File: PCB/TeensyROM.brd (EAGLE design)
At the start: 160 x 100 mm, 2 parts, among them P1 MA22-2, U1 TEENSY41-STRIP

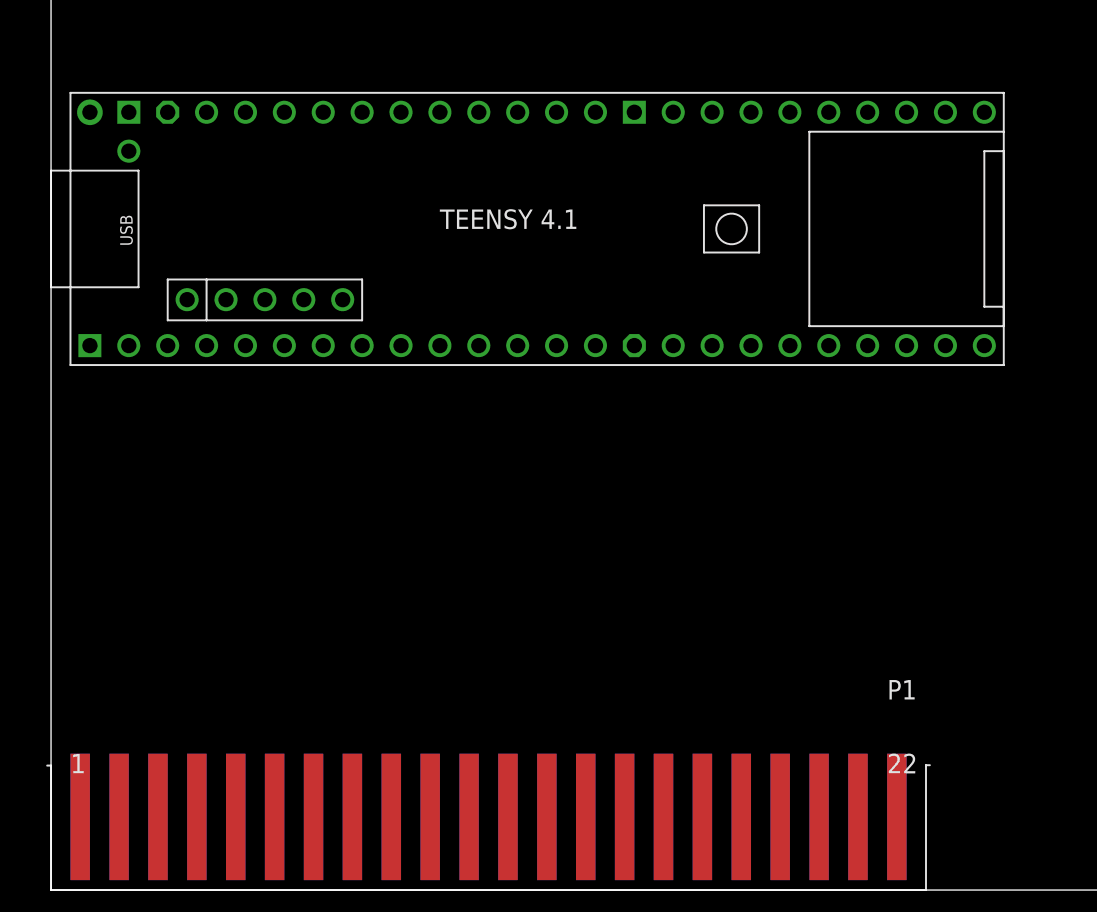
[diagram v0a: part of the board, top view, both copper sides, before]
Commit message: DMA/NMI pins
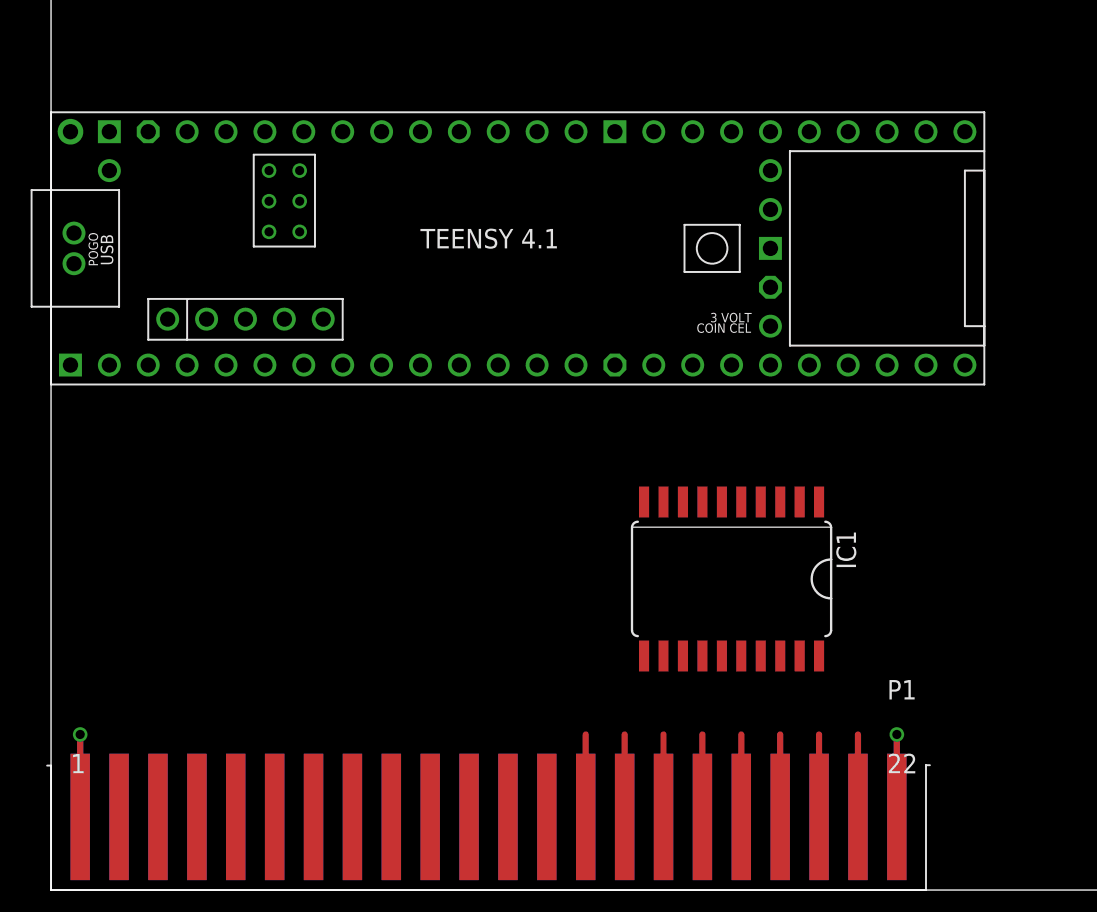
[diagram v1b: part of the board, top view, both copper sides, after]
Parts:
- removed U1: TEENSY41-STRIP, teensy:TEENSY41-STRIP
- added IC1: 74LS245DW, 74xx-us:SO20W
- added U$1: TEENSY41, teensy:TEENSY41
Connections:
- new net *DMA: P1.13
- new net *EXROM: P1.9
- new net *GAME: P1.8
- new net *IO1: P1.7
- new net *IO2: P1.10
- new net *IRQ: P1.4
- new net *NMI: P1.D
- new net *RESET: P1.C
- new net *ROMH: P1.B
- new net *ROML: P1.11
- new net +5V: P1.2, P1.3
- new net A0: P1.Y
- new net A1: P1.X
- new net A10: P1.M
- new net A11: P1.L
- new net A12: P1.K
- new net A13: P1.J
- new net A14: P1.H
- new net A15: P1.F
- new net A2: P1.W
- new net A3: P1.V
- new net A4: P1.U
- new net A5: P1.T
- new net A6: P1.S
- new net A7: P1.R
- new net A8: P1.P
- new net A9: P1.N
- new net BA: P1.12
- new net D0: IC1.18, P1.21
- new net D0_B: IC1.2, U$1.10-CS\MQSR
- new net D1: IC1.17, P1.20
- new net D1_B: IC1.3, U$1.11-MOSI/CTX1
- new net D2: IC1.16, P1.19
- new net D2_B: IC1.4, U$1.12-MISO/MQSL
- new net D3: IC1.15, P1.18
- new net D3_B: IC1.5, U$1.13-SCK/LED
- new net D4: IC1.14, P1.17
- new net D4_B: IC1.6, U$1.8-TX2/IN1
- new net D5: IC1.13, P1.16
- new net D5_B: IC1.7, U$1.7-RX2/OUT1A
- new net D6: IC1.12, P1.15
- new net D6_B: IC1.8, U$1.36-PWM
- new net D7: IC1.11, P1.14
- new net D7_B: IC1.9, U$1.37-PWM
- new net DOT_CLK: P1.6
- new net GND: IC1.10, P1.1, P1.22, P1.A, P1.Z
- new net PHI2: P1.E
- new net R/*W: P1.5
- new net VCC: IC1.20
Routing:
- net GND: track 0.00 -> 21.5 mm, vias 0 -> 2
- net D7: track 0.00 -> 5.38 mm
- net D6: track 0.00 -> 5.38 mm
- net D5: track 0.00 -> 5.38 mm
- net D4: track 0.00 -> 5.38 mm
- net D3: track 0.00 -> 5.38 mm
- net D2: track 0.00 -> 5.38 mm
- net D1: track 0.00 -> 5.38 mm
- net D0: track 0.00 -> 5.38 mm

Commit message: schem updates
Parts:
- removed P1: MA22-2, con-edge-100:44PINEDGE
- added B9: SW-MOM, AudioLooper:TACTILE-PTH
- added C1, C3: (no value), rcl:E2,5-6
- added C2: (no value), rcl:A/3216-18W
- added D5: RED, Dolphin v3.20:LED-3MM-PTH
- added D6: GRN, Dolphin v3.20:LED-3MM-PTH
- added IC2, IC3, IC4: 74LS245DW, 74xx-us:SO20W
- added IC5: 74LS07D, 74xx-us:SO14
- added J1: C64-EXPANSION-PORT, Commodore:EXPANSIO_SQ
- added J2: (no value), AudioLooper:USB
- added JP1: (no value), pinhead:2X22
- added R6: 4.7k, resistor:R0805
- added X1: SI-50170, con-stewart:SI-50170
- moved IC1 6.48 mm to (50.8, 19.1)
- moved U$1 1.27 mm to (31.8, 40.6)
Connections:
- removed net *DMA: P1.13
- removed net *EXROM: P1.9
- removed net *GAME: P1.8
- removed net *IO1: P1.7
- removed net *IO2: P1.10
- removed net *IRQ: P1.4
- removed net *NMI: P1.D
- removed net *RESET: P1.C
- removed net *ROMH: P1.B
- removed net *ROML: P1.11
- removed net R/*W: P1.5
- new net !DMA: J1.13
- new net !EXROM: J1.9
- new net !GAME: J1.8
- new net !IO1: J1.7
- new net !IO2: J1.10
- new net !IRQ: J1.4
- new net !NMI: J1.D
- new net !RESET: J1.C
- new net !ROMH: J1.B
- new net !ROML: J1.11
- new net +3V3: IC1.20, U$1.3V3-1, U$1.3V3-2, U$1.3V3-3
- new net +5V1: C1.+
- new net B12: D5.K
- new net D+: J2.D+
- new net D-: J2.D-
- new net GND1: J1.A, J1.Z
- new net GND2: D6.K
- new net GND3: C1.-
- new net N$1: D6.A, R6.1
- new net N$5: D5.A
- new net R/!W: J1.5
- new net USB5V: C2.+, J2.5V
- new net VCC1: R6.2
- net +5V: now also J1.2, J1.3; no longer P1.2, P1.3
- net A0: now also IC2.18, J1.Y; no longer P1.Y
- net A1: now also IC2.17, J1.X; no longer P1.X
- net A10: now also J1.M; no longer P1.M
- net A11: now also J1.L; no longer P1.L
- net A12: now also J1.K; no longer P1.K
- net A13: now also J1.J; no longer P1.J
- net A14: now also J1.H; no longer P1.H
- net A15: now also J1.F; no longer P1.F
- net A2: now also IC2.16, J1.W; no longer P1.W
- net A3: now also IC2.15, J1.V; no longer P1.V
- net A4: now also IC2.14, J1.U; no longer P1.U
- net A5: now also IC2.13, J1.T; no longer P1.T
- net A6: now also IC2.12, J1.S; no longer P1.S
- net A7: now also IC2.11, J1.R; no longer P1.R
- net A8: now also J1.P; no longer P1.P
- net A9: now also J1.N; no longer P1.N
- net BA: now also J1.12; no longer P1.12
- net D0: now also J1.21; no longer P1.21
- net D1: now also J1.20; no longer P1.20
- net D2: now also J1.19; no longer P1.19
- net D3: now also J1.18; no longer P1.18
- net D4: now also J1.17; no longer P1.17
- net D5: now also J1.16; no longer P1.16
- net D6: now also J1.15; no longer P1.15
- net D7: now also J1.14; no longer P1.14
- net DOT_CLK: now also J1.6; no longer P1.6
- net GND: now also C2.-, IC2.10, IC3.10, IC4.10, IC5.7, J1.1, J1.22, J2.GND, J2.SH1, J2.SH2, U$1.GND1, U$1.GND2, U$1.GND3, U$1.GND4, U$1.GND5, U$1.GND6; no longer P1.1, P1.22, P1.A, P1.Z
- net PHI2: now also J1.E; no longer P1.E
- net VCC: now also IC2.20, IC3.20, IC4.20, IC5.14; no longer IC1.20
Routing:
- net D0_B: track 0.00 -> 34.5 mm
- net D5_B: track 0.00 -> 33.5 mm
- net D4_B: track 0.00 -> 32.0 mm
- net D6_B: track 0.00 -> 31.0 mm, vias 0 -> 1
- net D1_B: track 0.00 -> 29.8 mm
- net A0: track 0.00 -> 27.6 mm, vias 0 -> 1
- net D7_B: track 0.00 -> 25.5 mm, vias 0 -> 1
- net D2_B: track 0.00 -> 24.0 mm
- net GND: track 21.5 -> 0.00 mm, vias 2 -> 0
- net A2: track 0.00 -> 18.3 mm, vias 0 -> 1
- net D7: track 5.38 -> 18.1 mm
- net D6: track 5.38 -> 16.6 mm
- net D5: track 5.38 -> 15.5 mm
- net D4: track 5.38 -> 14.0 mm
- net D3: track 5.38 -> 12.6 mm
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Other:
- board size 160 x 100 mm -> 73.7 x 76.2 mm
